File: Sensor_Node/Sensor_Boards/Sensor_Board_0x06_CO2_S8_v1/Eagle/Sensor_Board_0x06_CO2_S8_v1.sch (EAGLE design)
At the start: 15 parts, among them J1 M04_SMD_90, J3 M03_SMD_90, J4 ARDUINO_ISP, U1 SENSEAIR_S8_SMD, U2 ATMEGA328P_TQFP, Y1 8MHZ

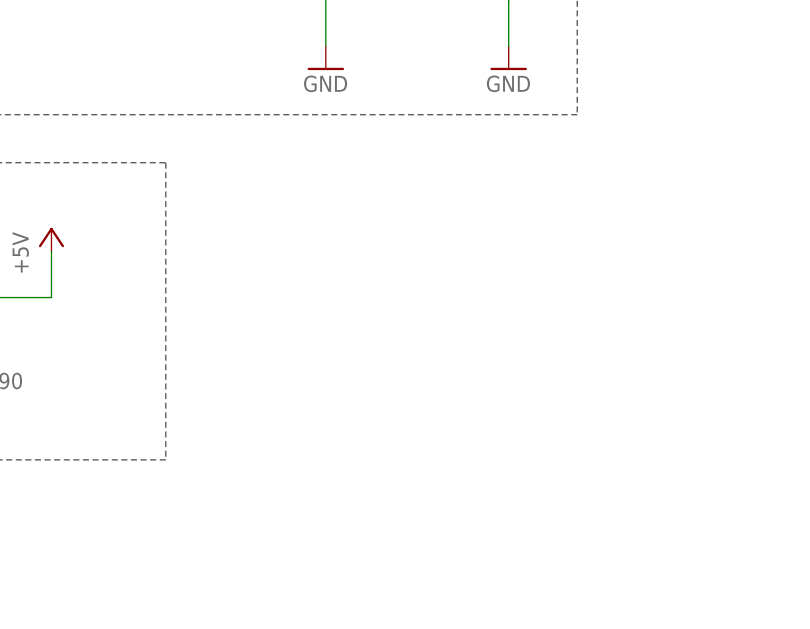
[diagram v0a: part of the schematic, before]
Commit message: Changes on SensModule CO2 S8
- added poppin programming connector
- moved communication connectors closer together
- turned C3
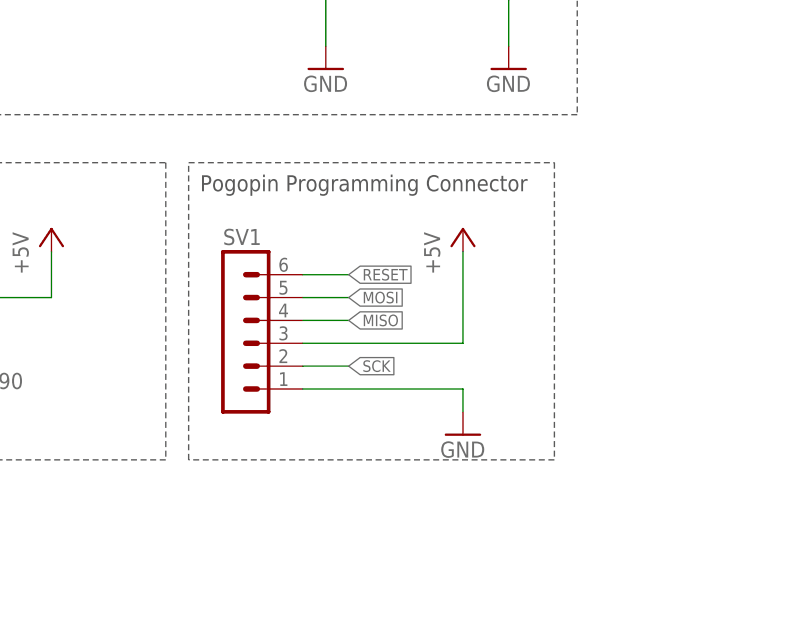
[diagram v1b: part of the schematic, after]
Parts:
- added SV1: (no value), con-lstb:MA06-1
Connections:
- net +5V: now also SV1.3
- net GND: now also SV1.1
- net MISO: now also SV1.4
- net MOSI: now also SV1.5
- net RESET: now also SV1.6
- net SCK: now also SV1.2
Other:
- note added: "Pogopin Programming Connector"
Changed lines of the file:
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@@
 <layers>
 <layer number="1" name="Top" color="4" fill="1" visible="no" active="no"/>
+<layer number="2" name="Route2" color="1" fill="3" visible="no" active="no"/>
+<layer number="3" name="Route3" color="4" fill="3" visible="no" active="no"/>
+<layer number="4" name="Route4" color="1" fill="4" visible="no" active="no"/>
+<layer number="5" name="Route5" color="4" fill="4" visible="no" active="no"/>
+<layer number="6" name="Route6" color="1" fill="8" visible="no" active="no"/>
+<layer number="7" name="Route7" color="4" fill="8" visible="no" active="no"/>
+<layer number="8" name="Route8" color="1" fill="2" visible="no" active="no"/>
+<layer number="9" name="Route9" color="4" fill="2" visible="no" active="no"/>
+<layer number="10" name="Route10" color="1" fill="7" visible="no" active="no"/>
+<layer number="11" name="Route11" color="4" fill="7" visible="no" active="no"/>
+<layer number="12" name="Route12" color="1" fill="5" visible="no" active="no"/>
+<layer number="13" name="Route13" color="4" fill="5" visible="no" active="no"/>
+<layer number="14" name="Route14" color="1" fill="6" visible="no" active="no"/>
+<layer number="15" name="Route15" color="4" fill="6" visible="no" active="no"/>
 <layer number="16" name="Bottom" color="1" fill="1" visible="no" active="no"/>
 <layer number="17" name="Pads" color="2" fill="1" visible="no" active="no"/>
@@
 <part name="U$22" library="myownthings" deviceset="N/C" device=""/>
 <part name="U$23" library="myownthings" deviceset="N/C" device=""/>
+<part name="SV1" library="con-lstb" deviceset="MA06-1" device=""/>
+<part name="GND6" library="SparkFun-Aesthetics" deviceset="GND" device=""/>
+<part name="P+5" library="supply1" deviceset="+5V" device=""/>
 </parts>
 <sheets>
@@
 <text x="224.549478125" y="11.498909375" size="2.54" layer="94" font="vector">Sensor Board - CO2</text>
 <text x="277.911478125" y="1.133621875" size="2.54" layer="94" font="vector">1.0</text>
+<wire x1="81.28" y1="30.226" x2="81.28" y2="63.246" width="0.1524" layer="97" style="shortdash"/>
+<wire x1="81.28" y1="63.246" x2="121.92" y2="63.246" width="0.1524" layer="97" style="shortdash"/>
+<wire x1="121.92" y1="63.246" x2="121.92" y2="30.226" width="0.1524" layer="97" style="shortdash"/>
+<wire x1="121.92" y1="30.226" x2="81.28" y2="30.226" width="0.1524" layer="97" style="shortdash"/>
+<text x="82.55" y="60.071" size="1.778" layer="97">Pogopin Programming Connector</text>
 </plain>
 <instances>
@@
 <instance part="U$22" gate="G$1" x="58.42" y="45.72"/>
 <instance part="U$23" gate="G$1" x="58.42" y="43.18"/>
+<instance part="SV1" gate="1" x="86.36" y="45.72"/>
+<instance part="GND6" gate="1" x="111.76" y="33.02"/>
+<instance part="P+5" gate="1" x="111.76" y="55.88"/>
 </instances>
 <busses>
@@
 <pinref part="S3" gate="G$1" pin="3"/>
 <wire x1="99.06" y1="88.9" x2="96.52" y2="88.9" width="0.1524" layer="91"/>
+</segment>
+<segment>
+<pinref part="GND6" gate="1" pin="GND"/>
+<wire x1="111.76" y1="35.56" x2="111.76" y2="38.1" width="0.1524" layer="91"/>
+<pinref part="SV1" gate="1" pin="1"/>
+<wire x1="111.76" y1="38.1" x2="93.98" y2="38.1" width="0.1524" layer="91"/>
 </segment>
 </net>
@@
 <pinref part="J4" gate="G$1" pin="RST"/>
 </segment>
+<segment>
+<pinref part="SV1" gate="1" pin="6"/>
+<wire x1="93.98" y1="50.8" x2="99.06" y2="50.8" width="0.1524" layer="91"/>
+<label x="99.06" y="50.8" size="1.27" layer="95" xref="yes"/>
+</segment>
 </net>
 <net name="SCK" class="0">
@@
 <pinref part="U2" gate="U$1" pin="PB5(SCK)"/>
 </segment>
+<segment>
+<pinref part="SV1" gate="1" pin="2"/>
+<wire x1="93.98" y1="40.64" x2="99.06" y2="40.64" width="0.1524" layer="91"/>
+<label x="99.06" y="40.64" size="1.27" layer="95" xref="yes"/>
+</segment>
 </net>
 <net name="MISO" class="0">
@@
 <pinref part="U2" gate="U$1" pin="PB4(MISO)"/>
 </segment>
+<segment>
+<pinref part="SV1" gate="1" pin="4"/>
+<wire x1="93.98" y1="45.72" x2="99.06" y2="45.72" width="0.1524" layer="91"/>
+<label x="99.06" y="45.72" size="1.27" layer="95" xref="yes"/>
+</segment>
 </net>
 <net name="MOSI" class="0">
@@
 <label x="98.8016375" y="134.887690625" size="1.27" layer="95" xref="yes"/>
 <pinref part="U2" gate="U$1" pin="PB3(MOSI/OC2)"/>
+</segment>
+<segment>
+<pinref part="SV1" gate="1" pin="5"/>
+<wire x1="93.98" y1="48.26" x2="99.06" y2="48.26" width="0.1524" layer="91"/>
+<label x="99.06" y="48.26" size="1.27" layer="95" xref="yes"/>
 </segment>
 </net>
@@
 <wire x1="66.04" y1="48.26" x2="66.04" y2="53.34" width="0.1524" layer="91"/>
 </segment>
-</net>
+<segment>
+<pinref part="P+5" gate="1" pin="+5V"/>
+<wire x1="111.76" y1="53.34" x2="111.76" y2="43.18" width="0.1524" layer="91"/>
+<pinref part="SV1" gate="1" pin="3"/>
+<wire x1="111.76" y1="43.18" x2="93.98" y2="43.18" width="0.1524" layer="91"/>
+</segment>
+</net>

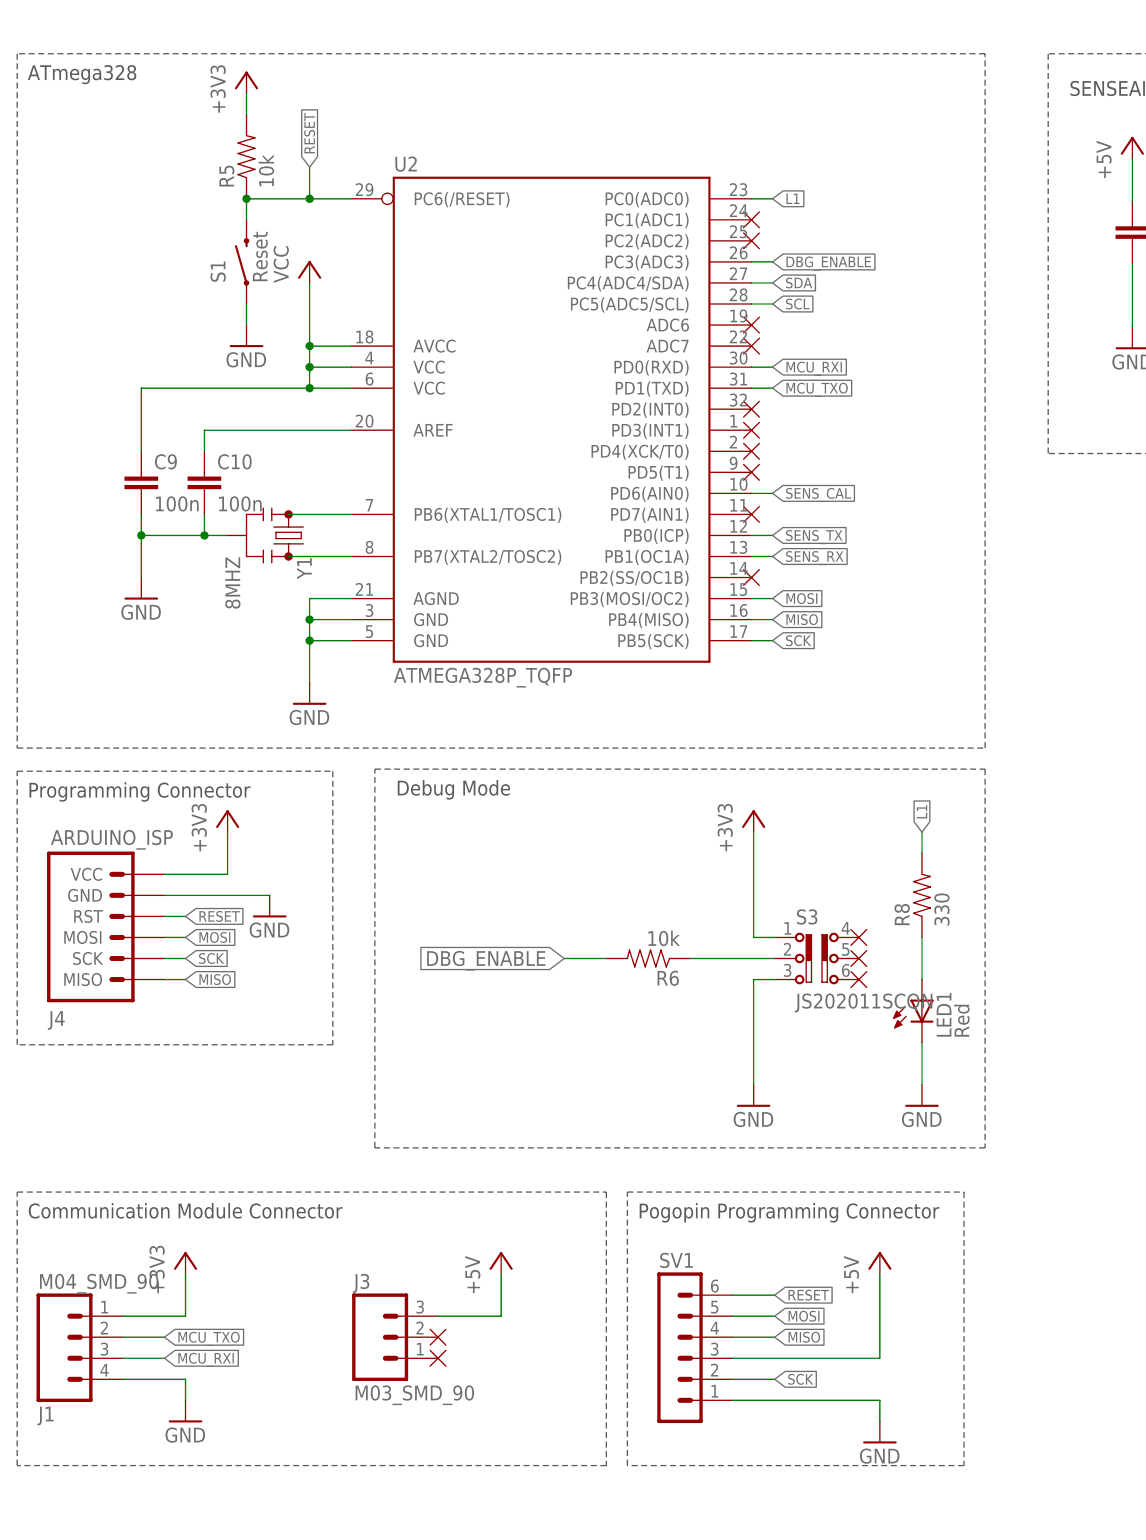
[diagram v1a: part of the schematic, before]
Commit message: Changes on all boards
- added capacitor on reset-path
- changed order of pogopin programmer pins

Pulse-Board:
- Deleted input-jumper. Currently one interrupt-pin missing, so print is
not yet routed.
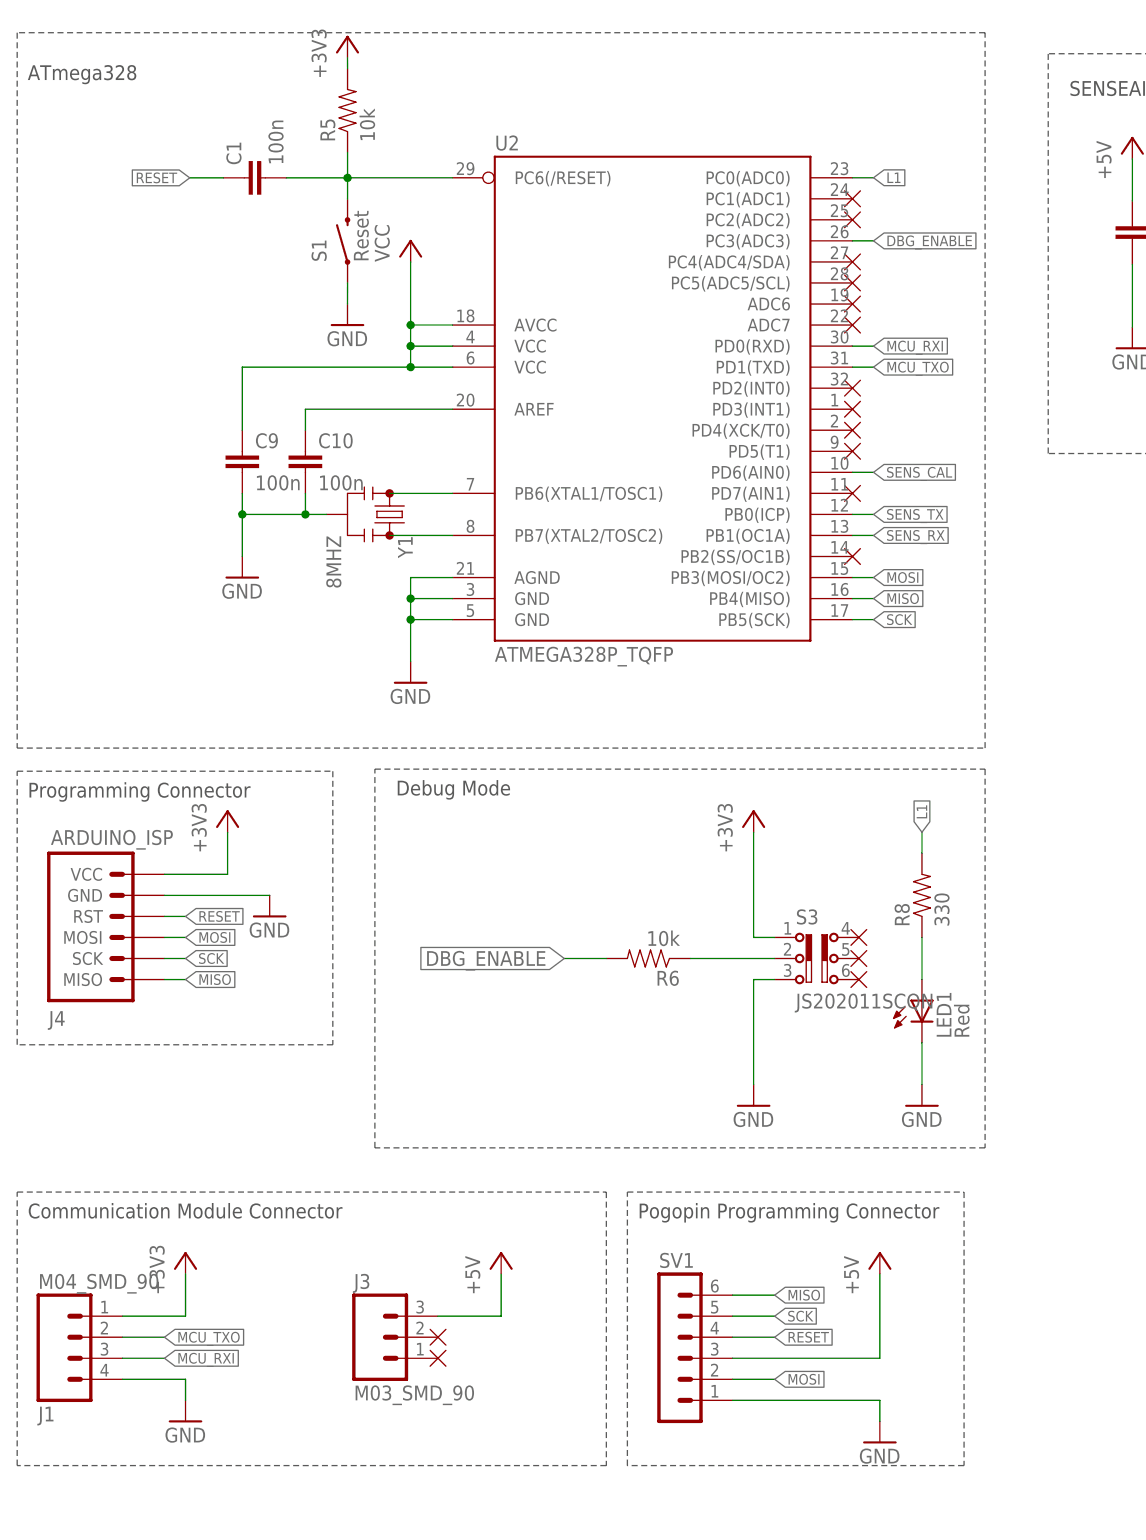
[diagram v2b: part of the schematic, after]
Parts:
- added C1: 100n, eagle-ltspice:C
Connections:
- removed net SCL: U2.PC5(ADC5/SCL)
- removed net SDA: U2.PC4(ADC4/SDA)
- new net N$9: C1.2, R5.1, S1.RIGHT, U2.PC6(/RESET)
- net MISO: now also SV1.6; no longer SV1.4
- net MOSI: now also SV1.2; no longer SV1.5
- net RESET: now also C1.1, SV1.4; no longer R5.1, S1.RIGHT, SV1.6, U2.PC6(/RESET)
- net SCK: now also SV1.5; no longer SV1.2
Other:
- moved on the sheet: C10, C9, R5, S1, U2, Y1

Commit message: Updated schematic description
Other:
- note added: "Sensor Board - CO2 (0x06)"
- note removed: "Sensor Board - CO2"
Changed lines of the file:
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@@
 <wire x1="220.98" y1="152.4" x2="132.08" y2="152.4" width="0.1524" layer="97" style="shortdash"/>
 <text x="134.62" y="195.58" size="1.778" layer="97">SENSEAIR_S8</text>
-<text x="224.549478125" y="11.498909375" size="2.54" layer="94" font="vector">Sensor Board - CO2</text>
+<text x="224.549478125" y="11.498909375" size="2.54" layer="94" font="vector">Sensor Board - CO2 (0x06)</text>
 <text x="277.911478125" y="1.133621875" size="2.54" layer="94" font="vector">1.0</text>
 <wire x1="81.28" y1="30.226" x2="81.28" y2="63.246" width="0.1524" layer="97" style="shortdash"/>

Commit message: Finished some boards.
- Minor changes on all boards except
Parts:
- removed SV1: (no value), con-lstb:MA06-1
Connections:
- net +5V: no longer SV1.3
- net GND: no longer SV1.1
- net MCU_RXI: now also U2.PB1(OC1A); no longer U2.PD0(RXD)
- net MCU_TXO: now also U2.PB0(ICP); no longer U2.PD1(TXD)
- net MISO: no longer SV1.6
- net MOSI: no longer SV1.2
- net RESET: no longer SV1.4
- net SCK: no longer SV1.5
- net SENS_RX: now also U2.PD1(TXD); no longer U2.PB1(OC1A)
- net SENS_TX: now also U2.PD0(RXD); no longer U2.PB0(ICP)
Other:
- note removed: "Pogopin Programming Connector"
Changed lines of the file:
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@@
 <part name="U$22" library="myownthings" deviceset="N/C" device=""/>
 <part name="U$23" library="myownthings" deviceset="N/C" device=""/>
-<part name="SV1" library="con-lstb" deviceset="MA06-1" device=""/>
-<part name="GND6" library="SparkFun-Aesthetics" deviceset="GND" device=""/>
-<part name="P+5" library="supply1" deviceset="+5V" device=""/>
 <part name="C1" library="eagle-ltspice" deviceset="C" device="" value="100n"/>
 <part name="U$16" library="myownthings" deviceset="N/C" device=""/>
@@
 <text x="224.549478125" y="11.498909375" size="2.54" layer="94" font="vector">Sensor Board - CO2 (0x06)</text>
 <text x="277.911478125" y="1.133621875" size="2.54" layer="94" font="vector">1.0</text>
-<wire x1="81.28" y1="30.226" x2="81.28" y2="63.246" width="0.1524" layer="97" style="shortdash"/>
-<wire x1="81.28" y1="63.246" x2="121.92" y2="63.246" width="0.1524" layer="97" style="shortdash"/>
-<wire x1="121.92" y1="63.246" x2="121.92" y2="30.226" width="0.1524" layer="97" style="shortdash"/>
-<wire x1="121.92" y1="30.226" x2="81.28" y2="30.226" width="0.1524" layer="97" style="shortdash"/>
-<text x="82.55" y="60.071" size="1.778" layer="97">Pogopin Programming Connector</text>
 </plain>
 <instances>
@@
 <instance part="U$22" gate="G$1" x="58.42" y="45.72"/>
 <instance part="U$23" gate="G$1" x="58.42" y="43.18"/>
-<instance part="SV1" gate="1" x="86.36" y="45.72"/>
-<instance part="GND6" gate="1" x="111.76" y="33.02"/>
-<instance part="P+5" gate="1" x="111.76" y="55.88"/>
 <instance part="C1" gate="G$1" x="35.052" y="185.674" rot="R90"/>
 <instance part="U$16" gate="G$1" x="108.4536375" y="172.987690625"/>
@@
 <pinref part="S3" gate="G$1" pin="3"/>
 <wire x1="99.06" y1="88.9" x2="96.52" y2="88.9" width="0.1524" layer="91"/>
-</segment>
-<segment>
-<pinref part="GND6" gate="1" pin="GND"/>
-<wire x1="111.76" y1="35.56" x2="111.76" y2="38.1" width="0.1524" layer="91"/>
-<pinref part="SV1" gate="1" pin="1"/>
-<wire x1="111.76" y1="38.1" x2="93.98" y2="38.1" width="0.1524" layer="91"/>
 </segment>
 </net>
@@
 <label x="28.448" y="185.674" size="1.27" layer="95" rot="R180" xref="yes"/>
 </segment>
-<segment>
-<pinref part="SV1" gate="1" pin="4"/>
-<wire x1="93.98" y1="45.72" x2="99.06" y2="45.72" width="0.1524" layer="91"/>
-<label x="99.06" y="45.72" size="1.27" layer="95" xref="yes"/>
-</segment>
 </net>
 <net name="SCK" class="0">
@@
 <pinref part="U2" gate="U$1" pin="PB5(SCK)"/>
 </segment>
-<segment>
-<pinref part="SV1" gate="1" pin="5"/>
-<wire x1="93.98" y1="48.26" x2="99.06" y2="48.26" width="0.1524" layer="91"/>
-<label x="99.06" y="48.26" size="1.27" layer="95" xref="yes"/>
-</segment>
 </net>
 <net name="MISO" class="0">
@@
 <pinref part="U2" gate="U$1" pin="PB4(MISO)"/>
 </segment>
-<segment>
-<pinref part="SV1" gate="1" pin="6"/>
-<wire x1="93.98" y1="50.8" x2="99.06" y2="50.8" width="0.1524" layer="91"/>
-<label x="99.06" y="50.8" size="1.27" layer="95" xref="yes"/>
-</segment>
 </net>
 <net name="MOSI" class="0">
@@
 <pinref part="U2" gate="U$1" pin="PB3(MOSI/OC2)"/>
 </segment>
-<segment>
-<pinref part="SV1" gate="1" pin="2"/>
-<wire x1="93.98" y1="40.64" x2="99.06" y2="40.64" width="0.1524" layer="91"/>
-<label x="99.06" y="40.64" size="1.27" layer="95" xref="yes"/>
-</segment>
 </net>
 <net name="MCU_TXO" class="0">
-<segment>
-<wire x1="108.4536375" y1="162.827690625" x2="110.9936375" y2="162.827690625" width="0.1524" layer="91"/>
-<label x="110.9936375" y="162.827690625" size="1.27" layer="95" xref="yes"/>
-<pinref part="U2" gate="U$1" pin="PD1(TXD)"/>
-</segment>
 <segment>
 <wire x1="20.32" y1="45.72" x2="25.4" y2="45.72" width="0.1524" layer="91"/>
@@
 <pinref part="J1" gate="G$1" pin="2"/>
 </segment>
+<segment>
+<pinref part="U2" gate="U$1" pin="PB0(ICP)"/>
+<wire x1="108.4536375" y1="145.047690625" x2="110.9936375" y2="145.047690625" width="0.1524" layer="91"/>
+<label x="110.9936375" y="145.047690625" size="1.27" layer="95" xref="yes"/>
+</segment>
 </net>
 <net name="L1" class="0">
@@
 <net name="MCU_RXI" class="0">
 <segment>
-<wire x1="108.4536375" y1="165.367690625" x2="110.9936375" y2="165.367690625" width="0.1524" layer="91"/>
-<label x="110.9936375" y="165.367690625" size="1.27" layer="95" xref="yes"/>
-<pinref part="U2" gate="U$1" pin="PD0(RXD)"/>
-</segment>
-<segment>
 <wire x1="20.32" y1="43.18" x2="25.4" y2="43.18" width="0.1524" layer="91"/>
 <label x="25.4" y="43.18" size="1.27" layer="95" xref="yes"/>
 <pinref part="J1" gate="G$1" pin="3"/>
+</segment>
+<segment>
+<pinref part="U2" gate="U$1" pin="PB1(OC1A)"/>
+<wire x1="108.4536375" y1="142.507690625" x2="110.9936375" y2="142.507690625" width="0.1524" layer="91"/>
+<label x="110.9936375" y="142.507690625" size="1.27" layer="95" xref="yes"/>
 </segment>
 </net>
@@
 </segment>
 <segment>
-<pinref part="U2" gate="U$1" pin="PB1(OC1A)"/>
-<wire x1="108.4536375" y1="142.507690625" x2="110.9936375" y2="142.507690625" width="0.1524" layer="91"/>
-<label x="110.9936375" y="142.507690625" size="1.27" layer="95" xref="yes"/>
+<wire x1="108.4536375" y1="162.827690625" x2="110.9936375" y2="162.827690625" width="0.1524" layer="91"/>
+<label x="110.9936375" y="162.827690625" size="1.27" layer="95" xref="yes"/>
+<pinref part="U2" gate="U$1" pin="PD1(TXD)"/>
 </segment>
 </net>
@@
 </segment>
 <segment>
-<pinref part="U2" gate="U$1" pin="PB0(ICP)"/>
-<wire x1="108.4536375" y1="145.047690625" x2="110.9936375" y2="145.047690625" width="0.1524" layer="91"/>
-<label x="110.9936375" y="145.047690625" size="1.27" layer="95" xref="yes"/>
+<wire x1="108.4536375" y1="165.367690625" x2="110.9936375" y2="165.367690625" width="0.1524" layer="91"/>
+<label x="110.9936375" y="165.367690625" size="1.27" layer="95" xref="yes"/>
+<pinref part="U2" gate="U$1" pin="PD0(RXD)"/>
 </segment>
 </net>
@@
 <wire x1="66.04" y1="48.26" x2="66.04" y2="53.34" width="0.1524" layer="91"/>
 </segment>
-<segment>
-<pinref part="P+5" gate="1" pin="+5V"/>
-<wire x1="111.76" y1="53.34" x2="111.76" y2="43.18" width="0.1524" layer="91"/>
-<pinref part="SV1" gate="1" pin="3"/>
-<wire x1="111.76" y1="43.18" x2="93.98" y2="43.18" width="0.1524" layer="91"/>
-</segment>
-</net>
+</net>
